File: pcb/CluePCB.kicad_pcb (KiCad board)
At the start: 2 copper layers, 78.7 x 81.3 mm, 11 parts, among them M3 MountingHole, U1 LoRa, U2 GPS, U3 Dragontail, U4 PowerBoost500, U5 Drag3V

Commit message: First take on PCB
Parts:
- removed M3 (x4): MountingHole, MountingHole:MountingHole_3.2mm_M3
- removed R1: 2.2k, Resistor_THT:R_Axial_DIN0204_L3.6mm_D1.6mm_P5.08mm_Horizontal
- removed R2: 3.3k, Resistor_THT:R_Axial_DIN0204_L3.6mm_D1.6mm_P5.08mm_Horizontal
- removed U5: Drag3V, HABET_Lib:Dragon3V
- added BT1: Battery_Cell, Battery:BatteryHolder_Keystone_1042_1x18650, F.Cu at (66.0, 94.0)
- added C1: 0.1uF, Capacitor_THT:C_Rect_L7.0mm_W4.5mm_P5.00mm, F.Cu at (99.7, 114.3)
- added C2: 0.1uF, Capacitor_THT:C_Rect_L7.0mm_W4.5mm_P5.00mm, F.Cu at (116.8, 96.5)
- added J1: Conn_01x02, Connector_PinHeader_2.54mm:PinHeader_1x02_P2.54mm_Vertical, F.Cu at (127.0, 132.1)
- added J2: Conn_01x02, Connector_PinHeader_2.54mm:PinHeader_1x02_P2.54mm_Vertical, F.Cu at (147.3, 132.1)
- added J3: Conn_01x02, Connector_PinHeader_2.54mm:PinHeader_1x02_P2.54mm_Vertical, F.Cu at (137.2, 132.1)
- added SW1: SW_SPST, Connector_PinHeader_2.54mm:PinHeader_1x02_P2.54mm_Vertical, F.Cu at (212.9, 72.2)
- U1: value LoRa -> Sparkfun_PRT-14411; footprint HABET_Lib:LoRa -> HAR:Sparkfun Boost BOB
- U2: value GPS -> AP2112K-3.3; footprint HABET_Lib:GPS -> Package_TO_SOT_SMD:SOT-23-5
- U3: value Dragontail -> Sparkfun_Microbit_BOB-16446; footprint HABET_Lib:Dragontail -> HAR:Sparkfun Microbit BOB
- U4: value PowerBoost500 -> Adafruit_RFM96W-3073; footprint HABET_Lib:Powerboost500 -> HAR:Adafruit LoRa BOB
- moved U2 107.7 mm to (116.8, 106.7)
- moved U1 99.5 mm to (94.0, 91.4)
- moved U3 28.1 mm to (152.4, 43.2), turned to 0 degrees
- moved U4 6.76 mm to (193.0, 78.7)
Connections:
- U1 pad 1: Net-(U1-Pad1) -> Net-(SW1-Pad1)
- U1 pad 2: Net-(U1-Pad2) -> Net-(SW1-Pad2)
- U1 pad 3: unconnected-(U1-Pad3) -> Net-(J1-Pad2)
- U1 pad 4: Net-(U1-Pad4) -> GND
- U1 pad 5: Net-(U1-Pad5) -> unconnected-(U1-Pad5)
- U1 pad 6: Net-(U1-Pad6) -> Net-(C1-Pad1)
- U1 pad 7: Net-(U1-Pad7) -> GND
- U1 pad 8: Net-(U1-Pad8) -> Net-(BT1-Pad1)
- U1 pad 9: Net-(U1-Pad9) -> GND
- U2 pad 1: (no net) -> Net-(C1-Pad1)
- U2 pad 2: (no net) -> GND
- U2 pad 3: (no net) -> Net-(J3-Pad1)
- U2 pad 4: (no net) -> unconnected-(U2-Pad4)
- U3 pad 13: Net-(U1-Pad5) -> Net-(U3-Pad13)
- U3 pad 14: Net-(U1-Pad6) -> Net-(U3-Pad14)
- U3 pad 15: Net-(U1-Pad7) -> Net-(U3-Pad15)
- U3 pad 16: Net-(U1-Pad8) -> Net-(U3-Pad16)
- U3 pad 17: unconnected-(U3-Pad17) -> (no net)
- U3 pad 18: unconnected-(U3-Pad18) -> (no net)
- U3 pad 19: Net-(U1-Pad2) -> unconnected-(U3-Pad19)
- U3 pad 2: Net-(U1-Pad9) -> Net-(U3-Pad2)
- U3 pad 20: Net-(U1-Pad1) -> unconnected-(U3-Pad20)
- U3 pad 21: unconnected-(U3-Pad21) -> GND
- U3 pad 8: Net-(U1-Pad4) -> Net-(U3-Pad8)
- U4 pad 1: unconnected-(U4-Pad1) -> Net-(C2-Pad1)
- U4 pad 2: unconnected-(U4-Pad2) -> GND
- U4 pad 3: Net-(R1-Pad2) -> Net-(U3-Pad8)
- U4 pad 4: unconnected-(U4-Pad4) -> Net-(U3-Pad13)
- U4 pad 5: unconnected-(U4-Pad5) -> Net-(U3-Pad14)
- U4 pad 6: unconnected-(U4-Pad6) -> Net-(U3-Pad15)
- U4 pad 7: unconnected-(U4-Pad7) -> Net-(U3-Pad16)
- U4 pad 8: unconnected-(U4-Pad8) -> Net-(U3-Pad2)
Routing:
- net Net-(U1-Pad9): track 49.2 -> 0.00 mm
- net Net-(U1-Pad8): track 47.2 -> 0.00 mm
- net Net-(U1-Pad7): track 37.1 -> 0.00 mm
- net Net-(U1-Pad6): track 26.9 -> 0.00 mm
- net Net-(U1-Pad1): track 19.2 -> 0.00 mm
- net Net-(U1-Pad4): track 19.1 -> 0.00 mm
- net Net-(U1-Pad2): track 19.0 -> 0.00 mm
- net Net-(U1-Pad5): track 10.3 -> 0.00 mm
- net Net-(R1-Pad1): track 9.09 -> 0.00 mm
- net Net-(R1-Pad2): track 5.36 -> 0.00 mm
- removed copper zone on B.Cu, net Net-(U1-Pad1)
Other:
- board outline removed
- board text removed: "HABET Clue Module"

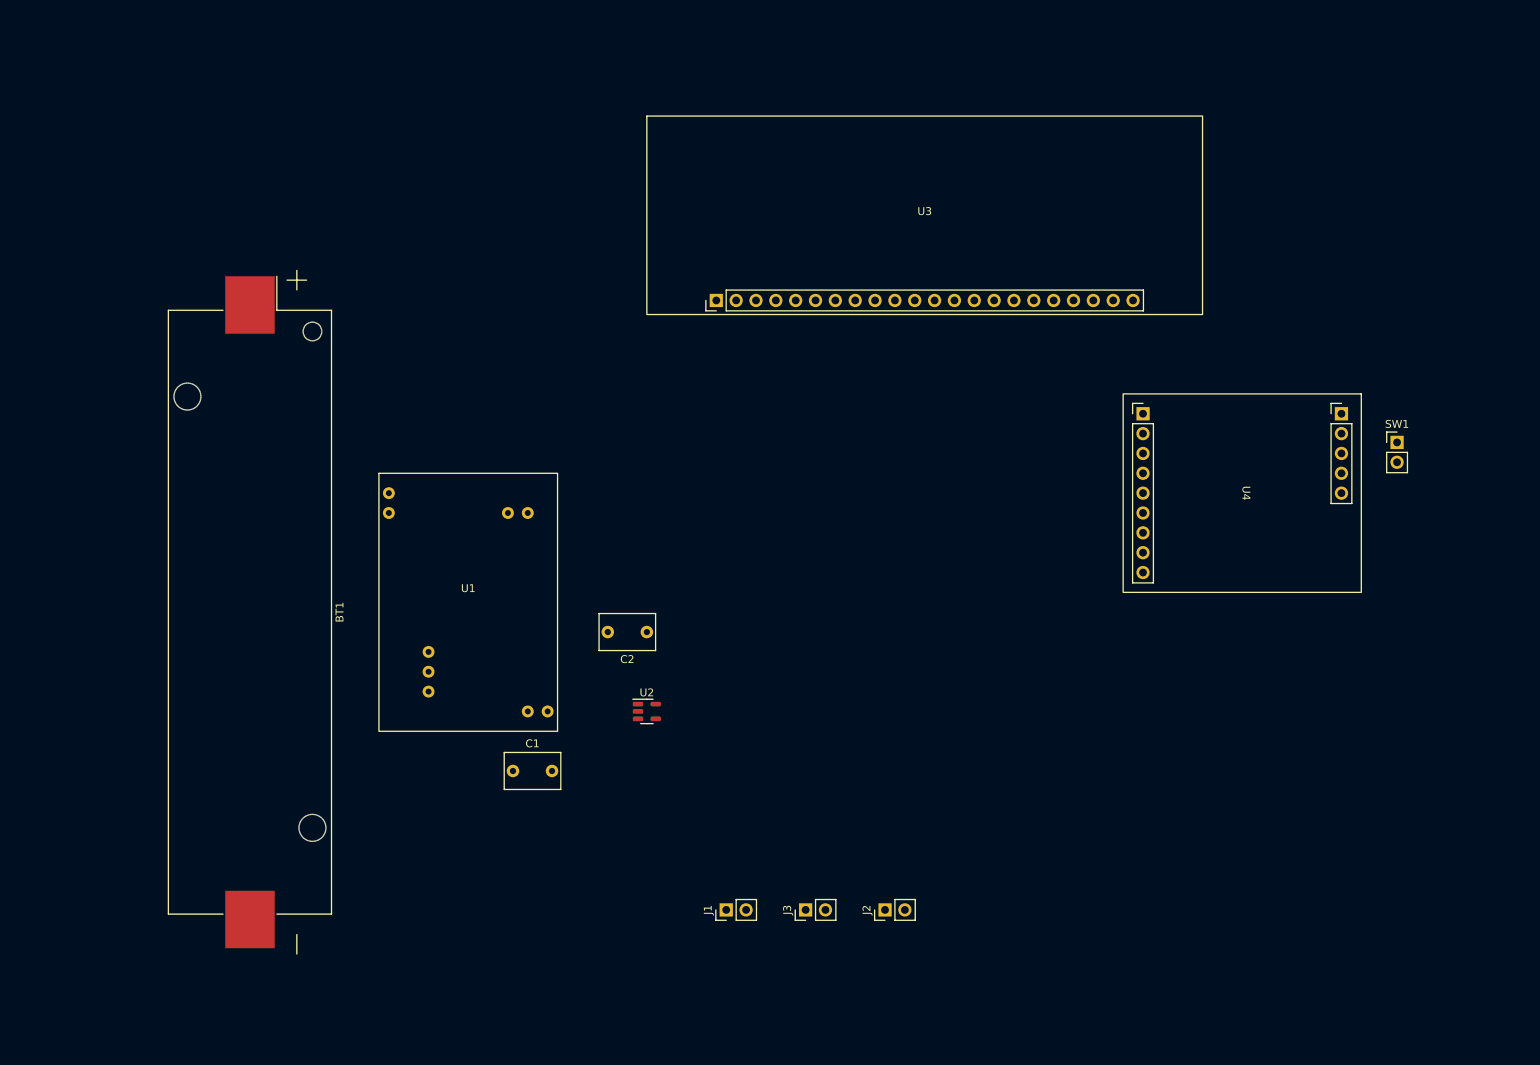
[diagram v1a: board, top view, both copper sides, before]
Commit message: Fixed some Footprints
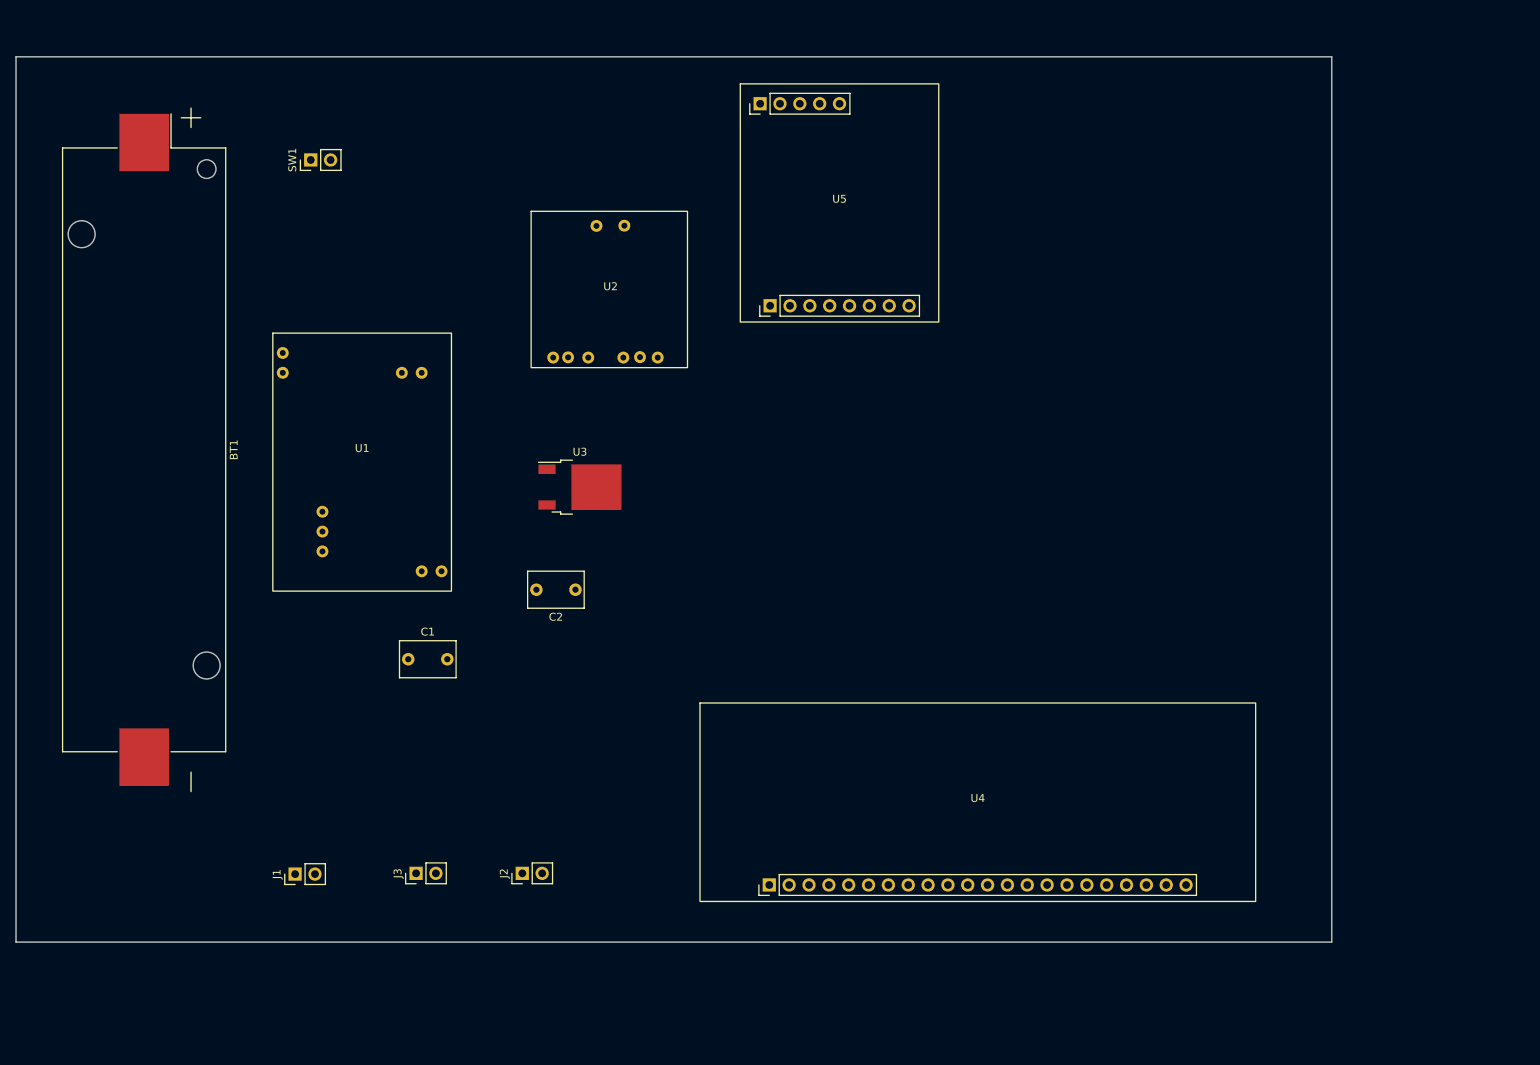
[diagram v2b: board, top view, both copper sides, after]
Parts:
- added U5: Adafruit_RFM96W-3073, HAR:Adafruit LoRa BOB, F.Cu at (141.5, 41.6)
- U2: value AP2112K-3.3 -> INA219-BOB; footprint Package_TO_SOT_SMD:SOT-23-5 -> HAR:INA219
- U3: value Sparkfun_Microbit_BOB-16446 -> AZ1117-3.3; footprint HAR:Sparkfun Microbit BOB -> Package_TO_SOT_SMD:TO-252-2
- U4: value Adafruit_RFM96W-3073 -> Sparkfun_Microbit_BOB-16446; footprint HAR:Adafruit LoRa BOB -> HAR:Sparkfun Microbit BOB
- moved SW1 143.7 mm to (73.8, 36.1), turned to 90 degrees
- moved U3 56.2 mm to (108.3, 78.0)
- moved J1 55.4 mm to (71.8, 127.5)
- moved U2 54.1 mm to (112.2, 52.8)
- moved U4 52.1 mm to (159.2, 118.3), turned to 0 degrees
- moved J3 50.1 mm to (87.3, 127.4)
- moved J2 46.7 mm to (100.9, 127.4)
- moved BT1 24.8 mm to (52.5, 73.2)
- moved U1 22.5 mm to (80.4, 73.5)
- moved C1 19.6 mm to (86.3, 100.0)
- moved C2 10.6 mm to (107.7, 91.1)
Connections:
- net Net-(BT1-Pad1) renamed +BATT
- net Net-(J1-Pad2) renamed +5V
- J2 pad 1: unconnected-(J2-Pad1) -> GND
- J2 pad 2: unconnected-(J2-Pad2) -> Net-(J2-Pad2)
- J3 pad 1: Net-(J3-Pad1) -> Net-(C2-Pad1)
- U1 pad 5: unconnected-(U1-Pad5) -> Net-(J2-Pad2)
- U2 pad 2: GND -> Net-(U2-Pad2)
- U2 pad 3: Net-(J3-Pad1) -> unconnected-(U2-Pad3)
- U2 pad 5: Net-(C2-Pad1) -> unconnected-(U2-Pad5)
- U3 pad 1: unconnected-(U3-Pad1) -> GND
- U3 pad 2: Net-(U3-Pad2) -> Net-(C2-Pad1)
- U3 pad 3: unconnected-(U3-Pad3) -> Net-(U2-Pad2)
- U4 pad 1: Net-(C2-Pad1) -> GND
- U4 pad 3: Net-(U3-Pad8) -> Net-(C2-Pad1)
- U4 pad 4: Net-(U3-Pad13) -> unconnected-(U4-Pad4)
- U4 pad 5: Net-(U3-Pad14) -> unconnected-(U4-Pad5)
- U4 pad 6: Net-(U3-Pad15) -> Net-(U4-Pad6)
- U4 pad 7: Net-(U3-Pad16) -> unconnected-(U4-Pad7)
- U4 pad 8: Net-(U3-Pad2) -> unconnected-(U4-Pad8)
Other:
- board outline added: 168.4 x 113.3 mm

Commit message: 1st draft on board
Board ready for first review. Added 3D parts into repo. LoRa does need some work for mounting holes
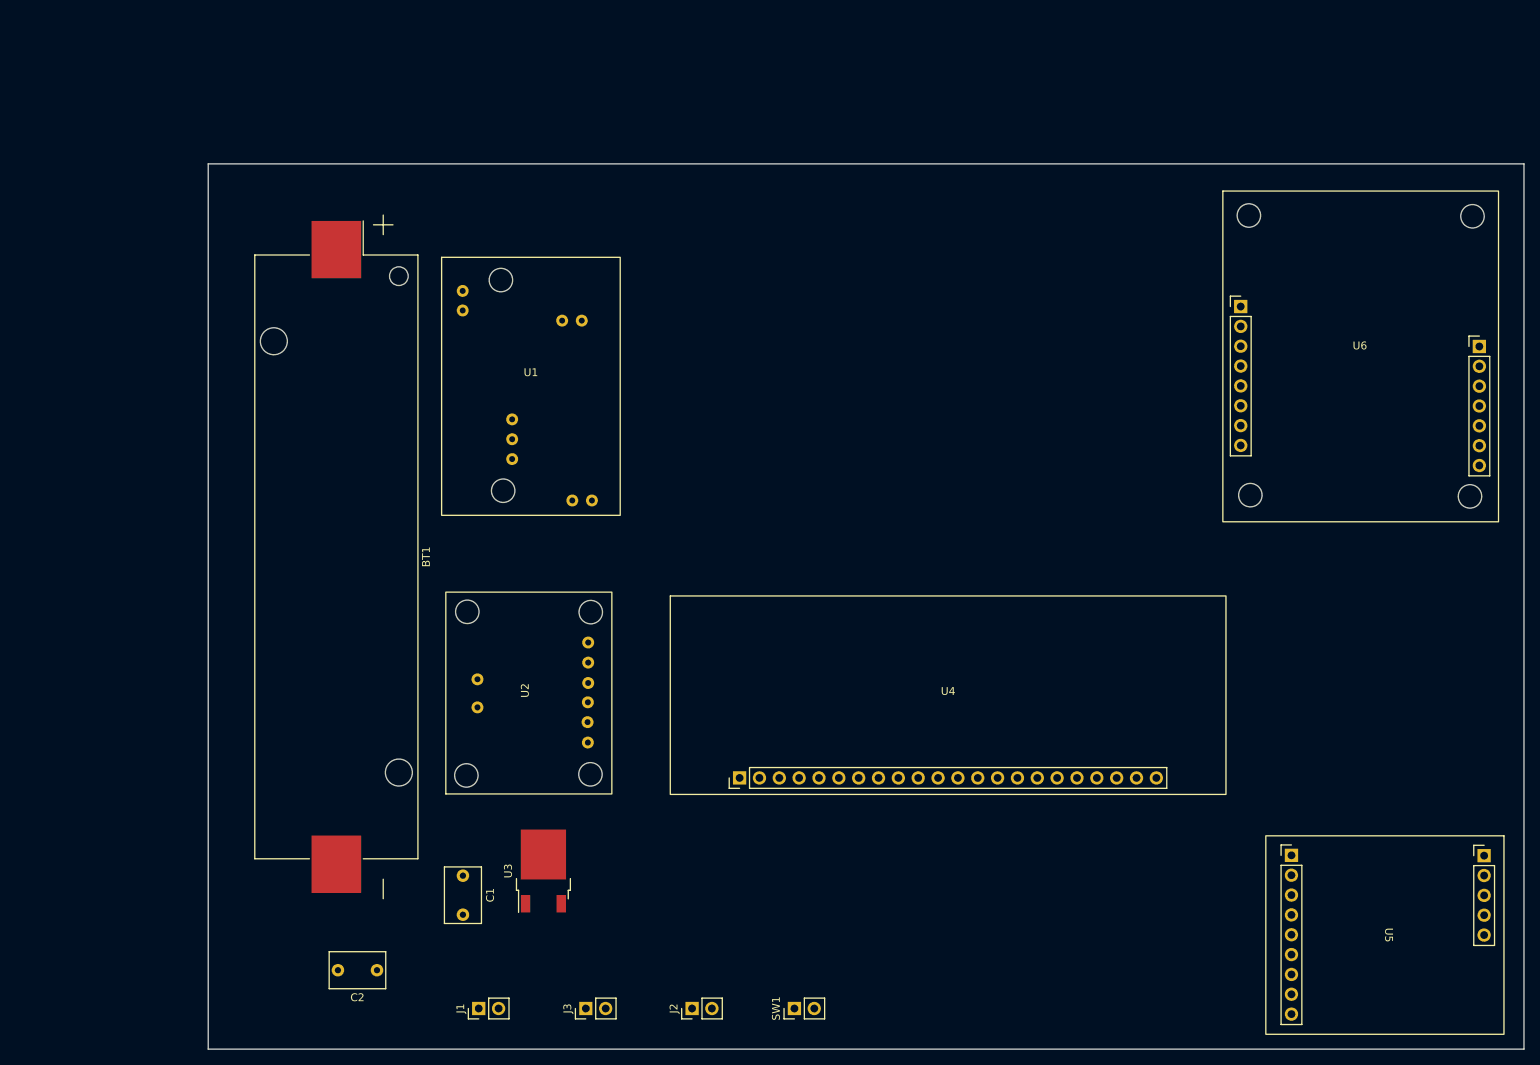
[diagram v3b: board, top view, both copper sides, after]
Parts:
- added U6: Sparkfun_GPS_NEO-M9N, HAR:Sparkfun GPS NEO M9N, F.Cu at (208.2, 63.7)
- moved SW1 125.0 mm to (135.7, 144.7)
- moved U5 116.8 mm to (211.3, 135.3), turned to -90 degrees
- moved C2 54.9 mm to (82.3, 139.8)
- moved U2 52.3 mm to (101.8, 104.0), turned to 90 degrees
- moved U3 49.3 mm to (103.6, 127.1), turned to 90 degrees
- moved J1 29.1 mm to (95.3, 144.7)
- moved C1 28.6 mm to (93.3, 127.7), turned to -90 degrees
- moved BT1 28.2 mm to (77.1, 86.9)
- moved J3 27.8 mm to (109.0, 144.7)
- moved J2 27.8 mm to (122.6, 144.7)
- moved U1 23.7 mm to (102.0, 63.8)
- moved U4 14.2 mm to (155.4, 104.6)
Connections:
- U5 pad 10: (no net) -> unconnected-(U5-Pad10)
- U5 pad 11: (no net) -> unconnected-(U5-Pad11)
- U5 pad 12: (no net) -> unconnected-(U5-Pad12)
- U5 pad 13: (no net) -> unconnected-(U5-Pad13)
- U5 pad 3: Net-(U4-Pad12) -> unconnected-(U5-Pad3)
- U5 pad 4: Net-(U4-Pad17) -> Net-(U4-Pad12)
- U5 pad 5: Net-(U4-Pad18) -> Net-(U4-Pad17)
- U5 pad 6: Net-(U4-Pad19) -> Net-(U4-Pad18)
- U5 pad 7: Net-(U4-Pad20) -> Net-(U4-Pad19)
- U5 pad 8: Net-(U4-Pad6) -> Net-(U4-Pad20)
- U5 pad 9: unconnected-(U5-Pad9) -> Net-(U4-Pad6)

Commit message: Updated LoRa, started routing
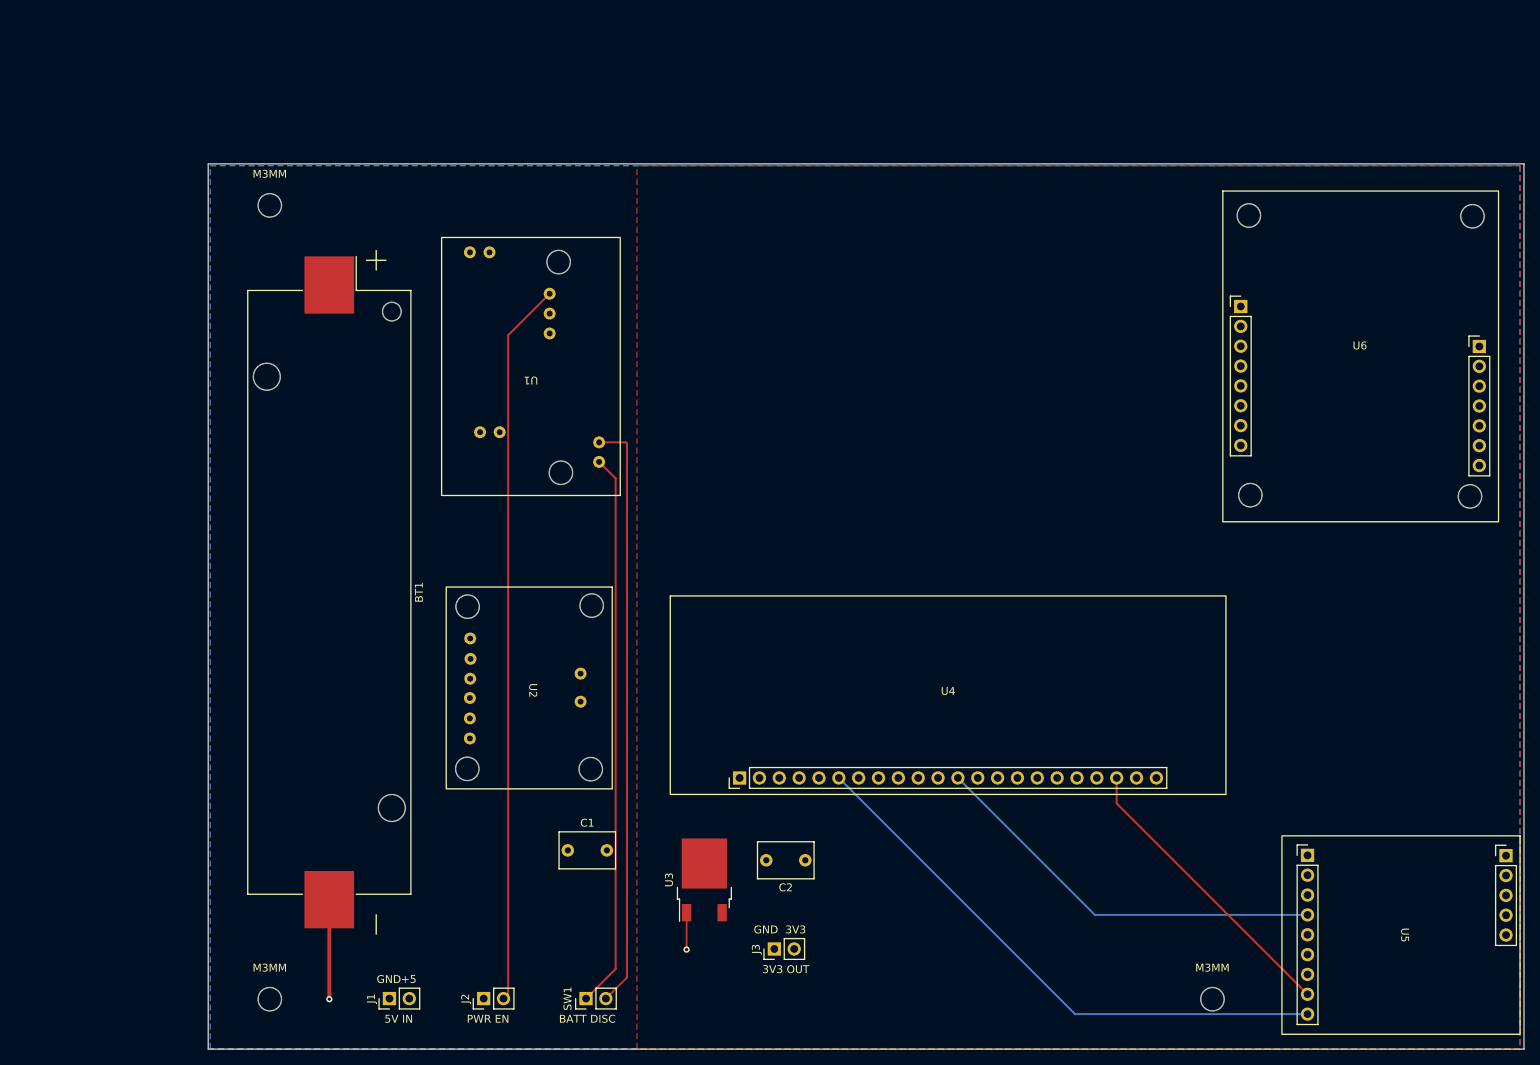
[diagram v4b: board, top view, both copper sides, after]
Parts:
- added M3MM: MountingHole_3mm, MountingHole:MountingHole_3mm, F.Cu at (68.6, 143.5)
- added M3MM: MountingHole_3mm, MountingHole:MountingHole_3mm, F.Cu at (189.2, 143.5)
- added M3MM: MountingHole_3mm, MountingHole:MountingHole_3mm, F.Cu at (68.6, 41.9)
- moved C2 56.6 mm to (137.1, 125.7)
- moved J2 26.7 mm to (96.0, 143.4)
- moved SW1 26.7 mm to (109.1, 143.4)
- moved J3 25.3 mm to (133.2, 137.1)
- moved U3 20.6 mm to (124.2, 128.2)
- moved C1 13.8 mm to (106.7, 124.5), turned to 0 degrees
- moved J1 11.5 mm to (83.9, 143.4)
- moved BT1 4.63 mm to (76.2, 91.4)
- moved U5 2.06 mm to (213.4, 135.3)
- turned U1 to 180 degrees
- turned U2 to -90 degrees
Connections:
- C2 pad 1: Net-(C2-Pad1) -> +3V3
- J3 pad 1: Net-(C2-Pad1) -> GND
- J3 pad 2: GND -> +3V3
- U3 pad 2: Net-(C2-Pad1) -> +3V3
- U4 pad 3: Net-(C2-Pad1) -> +3V3
- U5 pad 1: Net-(C2-Pad1) -> +3V3
- U6 pad 10: (no net) -> unconnected-(U6-Pad10)
- U6 pad 11: (no net) -> unconnected-(U6-Pad11)
- U6 pad 12: (no net) -> unconnected-(U6-Pad12)
- U6 pad 13: (no net) -> unconnected-(U6-Pad13)
- U6 pad 14: (no net) -> unconnected-(U6-Pad14)
- U6 pad 15: (no net) -> unconnected-(U6-Pad15)
- U6 pad 9: (no net) -> unconnected-(U6-Pad9)
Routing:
- net Net-(J2-Pad2): track 0.00 -> 92.7 mm
- net Net-(SW1-Pad2): track 0.00 -> 75.8 mm
- net Net-(U4-Pad6): track 0.00 -> 72.5 mm
- net Net-(SW1-Pad1): track 0.00 -> 71.1 mm
- net Net-(U4-Pad12): track 0.00 -> 52.0 mm
- net Net-(U4-Pad20): track 0.00 -> 37.8 mm
- net GND: track 0.00 -> 17.5 mm, vias 0 -> 2
- added copper zone on F.Cu, net +3V3
- added copper zone on B.Cu, net GND
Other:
- board text added: "+5"
- board text added: "3V3"
- board text added: "3V3 OUT"
- board text added: "5V IN"
- board text added: "BATT DISC"
- board text added: "GND"
- board text added: "PWR EN"

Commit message: 1st attempt at routing board
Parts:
- moved SW1 106.3 mm to (77.5, 41.9)
- moved U1 14.3 mm to (102.9, 49.5), turned to -90 degrees
- moved BT1 3.59 mm to (73.7, 94.0)
- renumbered M3MM to M3MM-1, M3MM to M3MM-2, M3MM to M3MM-3
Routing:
- net +5V: track 0.00 -> 100.8 mm
- net Net-(C1-Pad1): track 0.00 -> 80.2 mm
- net Net-(U4-Pad18): track 0.00 -> 57.4 mm
- net Net-(U4-Pad17): track 0.00 -> 56.2 mm
- net Net-(U4-Pad19): track 0.00 -> 54.8 mm
- net Net-(U2-Pad2): track 0.00 -> 48.8 mm
- net Net-(SW1-Pad2): track 75.8 -> 31.8 mm
- net +BATT: track 0.00 -> 36.8 mm
- net Net-(J2-Pad2): track 92.7 -> 128.4 mm
- net Net-(SW1-Pad1): track 71.1 -> 37.7 mm
- net Net-(U4-Pad12): track 52.0 -> 66.3 mm
- net Net-(U4-Pad20): track 37.8 -> 49.8 mm
- net GND: track 17.5 -> 18.4 mm, vias 2 -> 1
